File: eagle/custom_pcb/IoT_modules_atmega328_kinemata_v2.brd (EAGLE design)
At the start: 50 x 35 mm, 54 parts, among them IC2 4093DT, Q3 MOSFET-P, T1 2N2222, U2 ATMEGA328P, U3 FT232RL-BASICSSOP, U4 MCP73831, Y2 8MHz

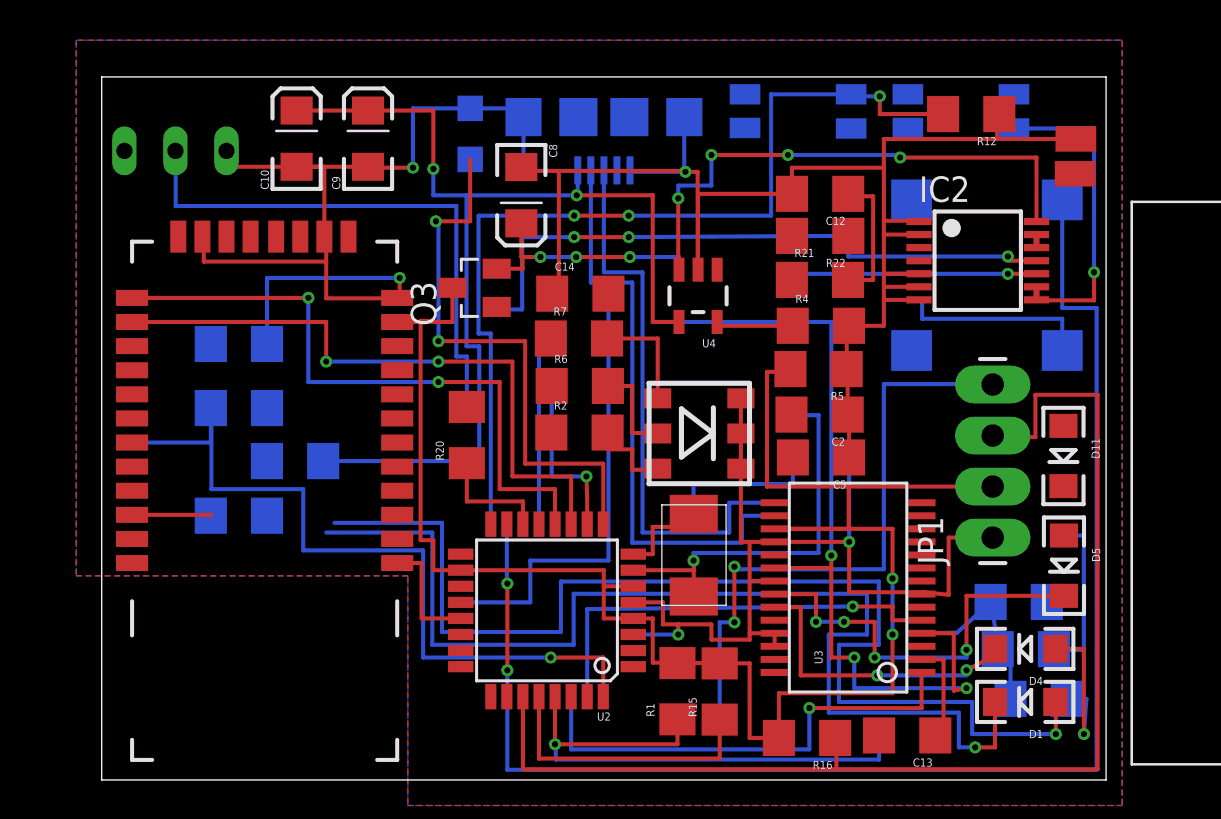
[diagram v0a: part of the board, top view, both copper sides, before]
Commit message: custom PCB wiring technically done, DRC ok
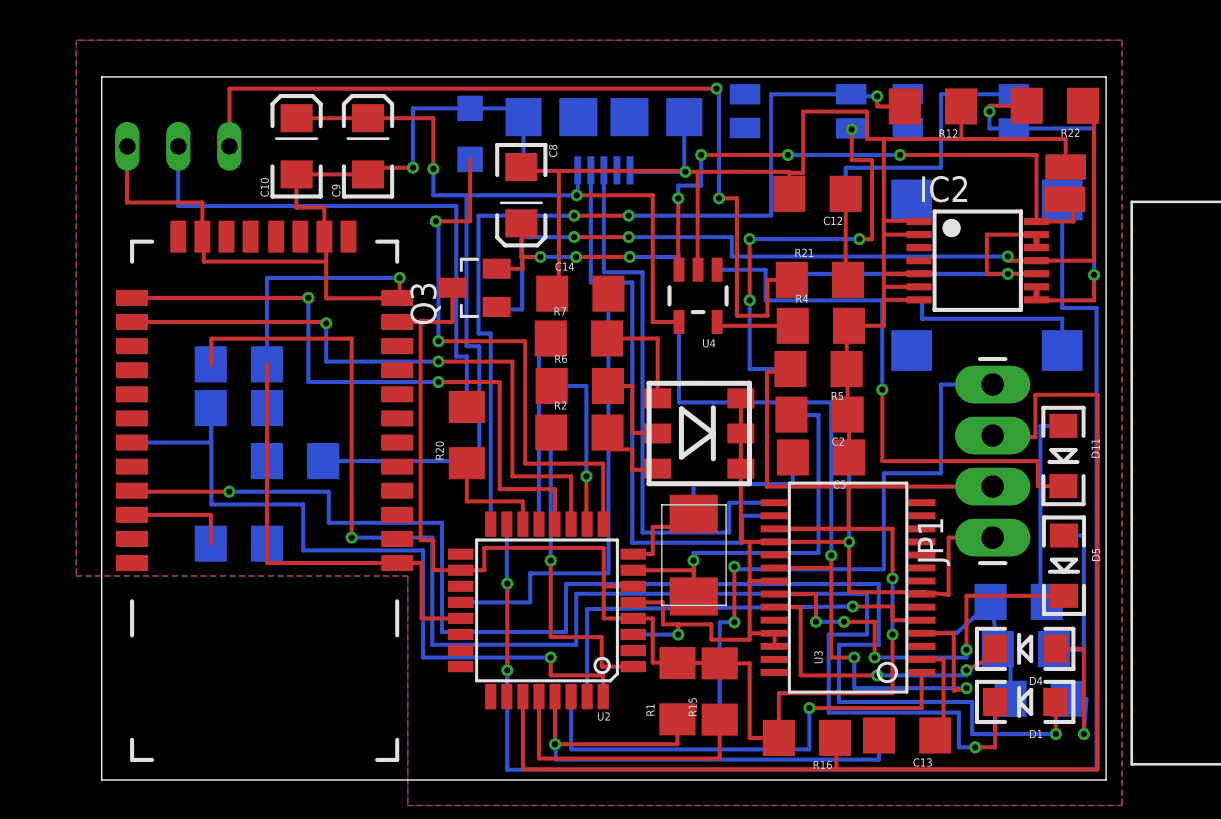
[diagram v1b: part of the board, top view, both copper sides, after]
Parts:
- moved R22 13.4 mm to (47.5, 33.6)
- moved T1 2.32 mm to (3.82, 30.3), turned to 180 degrees
- moved R12 1.94 mm to (41.4, 33.5)
- moved BAT-1 1.49 mm to (48.0, 30.5)
- moved R10 1.40 mm to (6.83, 11.8)
- moved BAT+2 1.37 mm to (48.0, 28.9)
- moved R9 1.02 mm to (6.83, 20.7)
- moved C10 0.38 mm to (9.70, 31.5)
- moved C9 0.38 mm to (13.3, 31.5)
- moved C12 0.13 mm to (35.6, 29.2)
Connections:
- removed net INT2: U2.22
- removed net RGB_B: U2.1
- net LED_B: now also U2.1
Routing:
- net N$23: track 13.1 -> 62.7 mm, vias 1 -> 3
- net STAT: track 0.00 -> 28.0 mm, vias 0 -> 1
- net 3.3V: track 91.1 -> 114.7 mm, vias 2 -> 6
- net GND: track 193.4 -> 216.5 mm
- net N$17: track 55.1 -> 71.8 mm, vias 1 -> 2
- net LED_B: track 0.00 -> 15.8 mm, vias 0 -> 1
- net N$13: track 57.0 -> 68.5 mm, vias 1 -> 2
- net N$27: track 31.8 -> 42.9 mm
- net PWR2: track 6.77 -> 17.7 mm
- net N$3: track 0.00 -> 10.2 mm
- net PWR1: track 16.1 -> 20.3 mm, vias 1 -> 2
- net VCC: track 38.9 -> 42.6 mm
- net BUTTON: track 46.1 -> 43.8 mm
- net N$12: track 3.96 -> 5.36 mm
